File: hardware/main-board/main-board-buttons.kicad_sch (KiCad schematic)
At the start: 29 parts, among them SW1 SW_Push, SW2 SW_Push, SW3 SW_Push, SW4 SW_Push, SW5 SW_Detect, SW6 SW_Boot

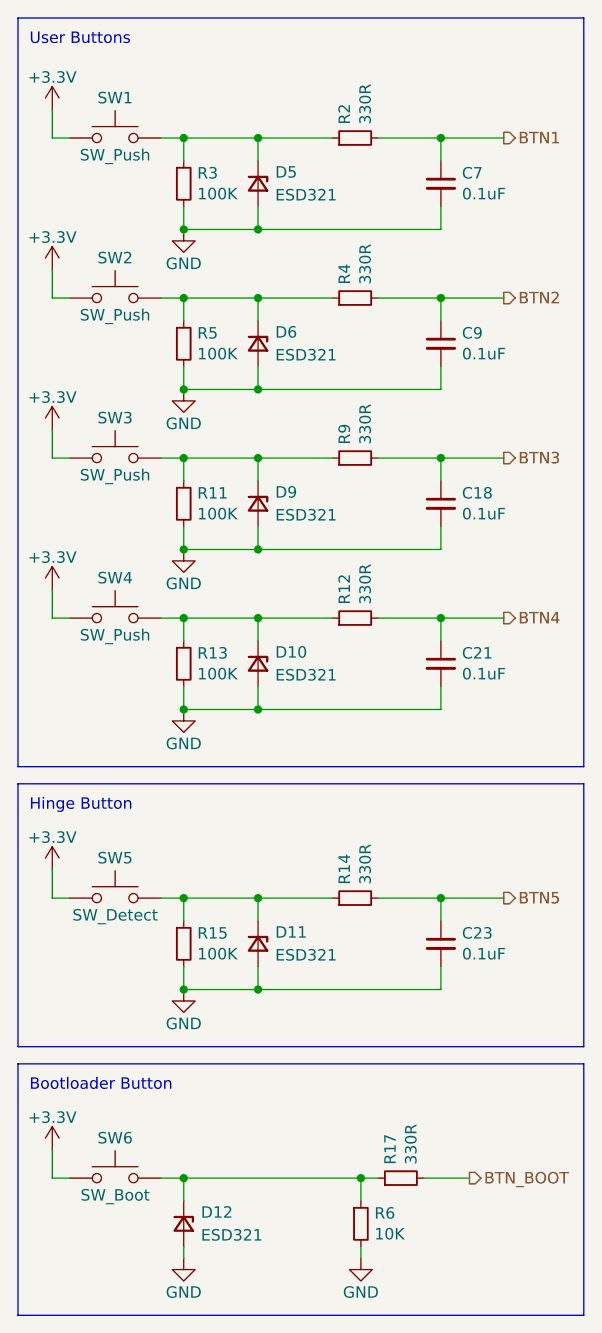
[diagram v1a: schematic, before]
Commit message: Update ESD321 symbols and footprints
Correct the library symbols and footprints used for the ESD321DYAR so
that the reversed pin 1 indiciation of these components still gets
assembled correctly.

Keeping the existing diode footprint with its marking, and adding a
supplemental dot to indicate how pin 1 differs from what this footprint
otherwise suggests.

This should make all the data correct, though an extra note in assembly
guidance will be necessary just in case.

Fix #1
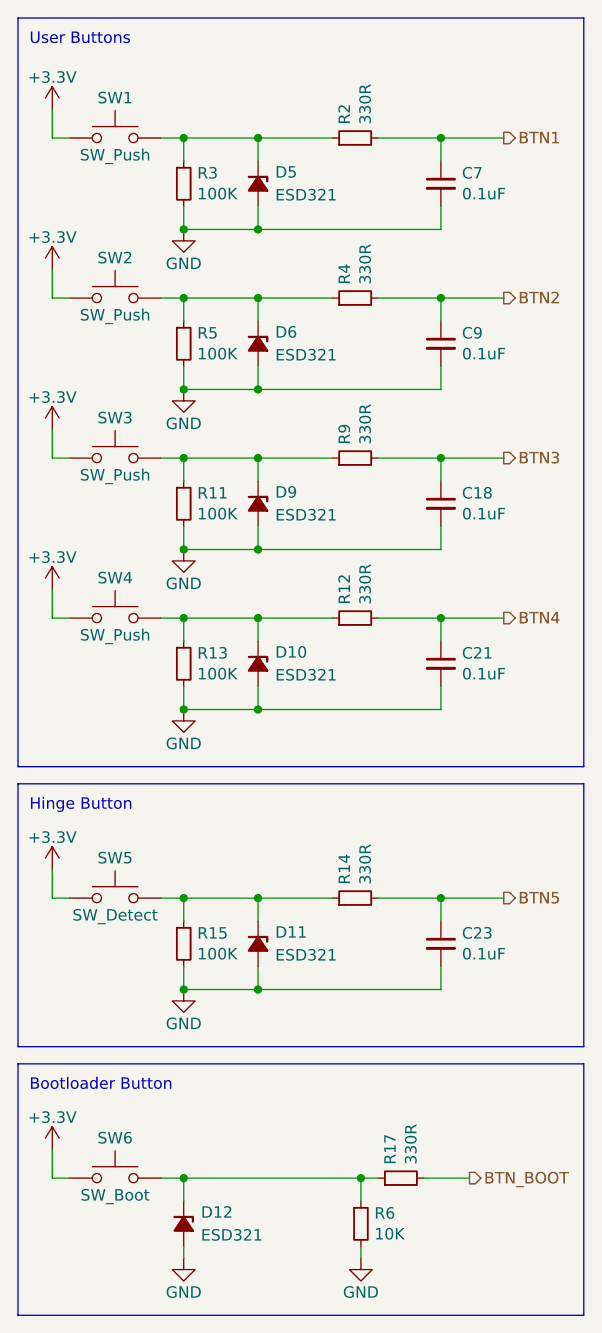
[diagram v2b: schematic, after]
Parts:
- D10, D11, D12, D5, D6, D9: symbol Device:D_Zener_Small -> Project:ESD321DYAR
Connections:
- net GND: now also D10.1 (A), D11.1 (A), D12.1 (A), D5.1 (A), D6.1 (A), D9.1 (A); no longer D10.2 (A), D11.2 (A), D12.2 (A), D5.2 (A), D6.2 (A), D9.2 (A)
- net at R14.1, R15.1, SW5.2: now also D11.2 (K); no longer D11.1 (K)
- net at R11.1, R9.1, SW3.2: now also D9.2 (K); no longer D9.1 (K)
- net at R4.1, R5.1, SW2.2: now also D6.2 (K); no longer D6.1 (K)
- net at R12.1, R13.1, SW4.2: now also D10.2 (K); no longer D10.1 (K)
- net at R17.1, R6.1, SW6.2: now also D12.2 (K); no longer D12.1 (K)
- net at R2.1, R3.1, SW1.2: now also D5.2 (K); no longer D5.1 (K)
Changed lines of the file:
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@@
 	(title_block
 		(title "Printalyzer UV/VIS Densitometer - Main Board")
-		(date "2024-09-24")
+		(date "2024-10-24")
 		(rev "C")
 		(company "Dektronics, Inc.")
@@
 	)
 	(symbol
-		(lib_id "Device:D_Zener_Small")
+		(lib_id "Project:ESD321DYAR")
 		(at 33.02 148.59 270)
 		(unit 1)
@@
 		)
 		(property "Footprint" "lib_fp:D_TI_SOD-523_DYA0002A"
-			(at 33.02 148.59 90)
+			(at 25.146 148.59 0)
 			(effects
 				(font
@@
 		)
 		(property "Datasheet" "https://www.ti.com/lit/ds/symlink/esd321.pdf"
-			(at 33.02 148.59 90)
+			(at 22.606 148.59 0)
 			(effects
 				(font
@@
 		)
 		(property "Description" "TVS DIODE 3.6VWM 6.3VC SOD523"
-			(at 33.02 148.59 0)
+			(at 27.686 148.59 0)
 			(effects
 				(font
@@
 	)
 	(symbol
-		(lib_id "Device:D_Zener_Small")
+		(lib_id "Project:ESD321DYAR")
 		(at 41.275 33.02 270)
 		(unit 1)
@@
 		)
 		(property "Footprint" "lib_fp:D_TI_SOD-523_DYA0002A"
-			(at 41.275 33.02 90)
+			(at 33.401 33.02 0)
 			(effects
 				(font
@@
 		)
 		(property "Datasheet" "https://www.ti.com/lit/ds/symlink/esd321.pdf"
-			(at 41.275 33.02 90)
+			(at 30.861 33.02 0)
 			(effects
 				(font
@@
 		)
 		(property "Description" "TVS DIODE 3.6VWM 6.3VC SOD523"
-			(at 41.275 33.02 0)
+			(at 35.941 33.02 0)
 			(effects
 				(font
@@
 	)
 	(symbol
-		(lib_id "Device:D_Zener_Small")
+		(lib_id "Project:ESD321DYAR")
 		(at 41.275 86.36 270)
 		(unit 1)
@@
 		)
 		(property "Footprint" "lib_fp:D_TI_SOD-523_DYA0002A"
-			(at 41.275 86.36 90)
+			(at 33.401 86.36 0)
 			(effects
 				(font
@@
 		)
 		(property "Datasheet" "https://www.ti.com/lit/ds/symlink/esd321.pdf"
-			(at 41.275 86.36 90)
+			(at 30.861 86.36 0)
 			(effects
 				(font
@@
 		)
 		(property "Description" "TVS DIODE 3.6VWM 6.3VC SOD523"
-			(at 41.275 86.36 0)
+			(at 35.941 86.36 0)
 			(effects
 				(font
@@
 	)
 	(symbol
-		(lib_id "Device:D_Zener_Small")
+		(lib_id "Project:ESD321DYAR")
 		(at 41.275 68.58 270)
 		(unit 1)
@@
 		)
 		(property "Footprint" "lib_fp:D_TI_SOD-523_DYA0002A"
-			(at 41.275 68.58 90)
+			(at 33.401 68.58 0)
 			(effects
 				(font
@@
 		)
 		(property "Datasheet" "https://www.ti.com/lit/ds/symlink/esd321.pdf"
-			(at 41.275 68.58 90)
+			(at 30.861 68.58 0)
 			(effects
 				(font
@@
 		)
 		(property "Description" "TVS DIODE 3.6VWM 6.3VC SOD523"
-			(at 41.275 68.58 0)
+			(at 35.941 68.58 0)
 			(effects
 				(font
@@
 	)
 	(symbol
-		(lib_id "Device:D_Zener_Small")
+		(lib_id "Project:ESD321DYAR")
 		(at 41.275 117.475 270)
 		(unit 1)
@@
 		)
 		(property "Footprint" "lib_fp:D_TI_SOD-523_DYA0002A"
-			(at 41.275 117.475 90)
+			(at 33.401 117.475 0)
 			(effects
 				(font
@@
 		)
 		(property "Datasheet" "https://www.ti.com/lit/ds/symlink/esd321.pdf"
-			(at 41.275 117.475 90)
+			(at 30.861 117.475 0)
 			(effects
 				(font
@@
 		)
 		(property "Description" "TVS DIODE 3.6VWM 6.3VC SOD523"
-			(at 41.275 117.475 0)
+			(at 35.941 117.475 0)
 			(effects
 				(font
@@
 	)
 	(symbol
-		(lib_id "Device:D_Zener_Small")
+		(lib_id "Project:ESD321DYAR")
 		(at 41.275 50.8 270)
 		(unit 1)
@@
 		)
 		(property "Footprint" "lib_fp:D_TI_SOD-523_DYA0002A"
-			(at 41.275 50.8 90)
+			(at 33.401 50.8 0)
 			(effects
 				(font
@@
 		)
 		(property "Datasheet" "https://www.ti.com/lit/ds/symlink/esd321.pdf"
-			(at 41.275 50.8 90)
+			(at 30.861 50.8 0)
 			(effects
 				(font
@@
 		)
 		(property "Description" "TVS DIODE 3.6VWM 6.3VC SOD523"
-			(at 41.275 50.8 0)
+			(at 35.941 50.8 0)
 			(effects
 				(font
